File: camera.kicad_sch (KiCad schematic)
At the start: 23 parts, among them J3 WE_68715014522, U10 PI4MSD5V9540BUEX, U11 AP7340-18FS4-7

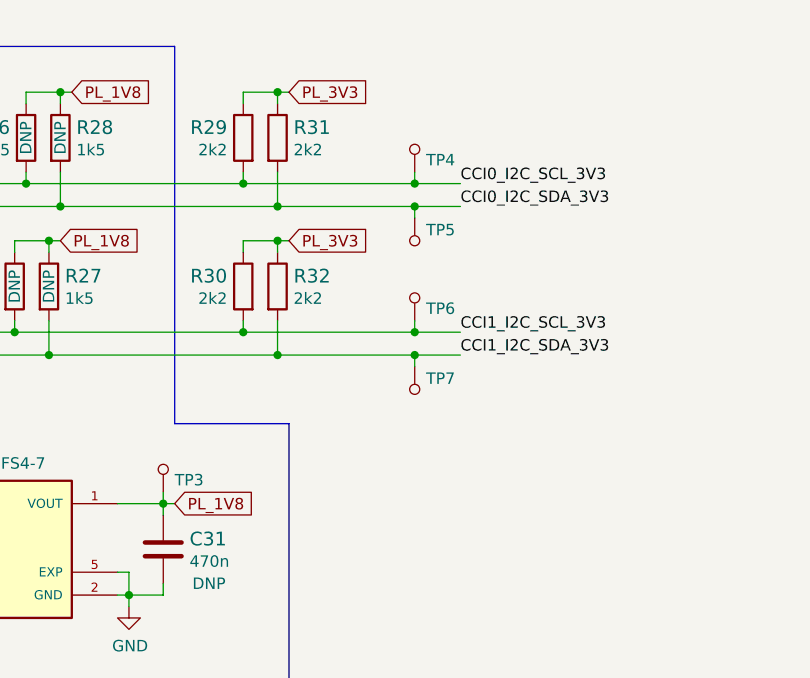
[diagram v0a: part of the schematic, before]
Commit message: Added cosmetic changes to schematics (e.g. position of labels, designators)
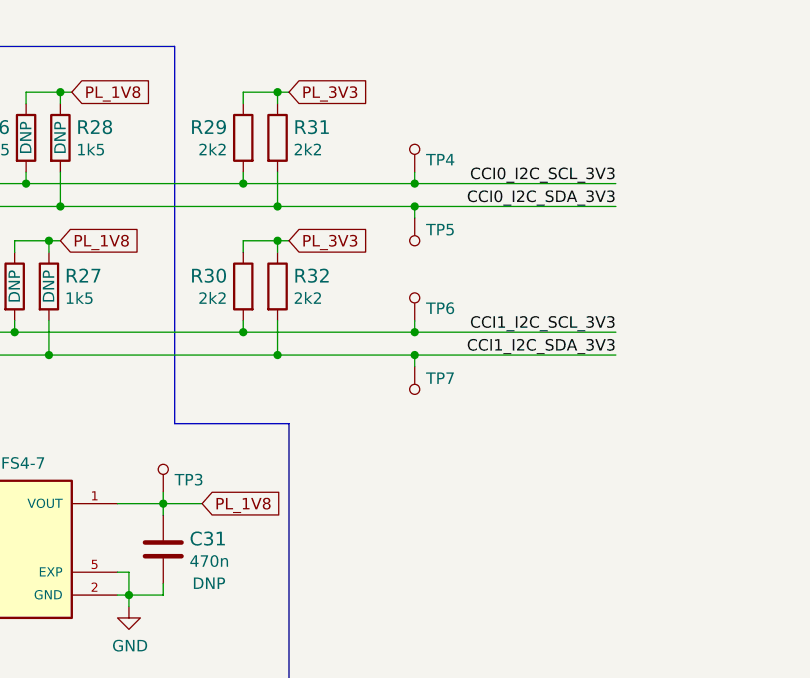
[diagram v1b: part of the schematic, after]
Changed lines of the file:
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@@
     (stroke (width 0) (type default) (color 0 0 0 0))
   )
-  (wire (pts (xy 111.76 149.86) (xy 113.03 149.86))
+  (wire (pts (xy 111.76 149.86) (xy 116.078 149.86))
     (stroke (width 0) (type default) (color 0 0 0 0))
   )
@@
     (stroke (width 0) (type default) (color 0 0 0 0))
   )
-  (wire (pts (xy 139.7 133.35) (xy 144.78 133.35))
+  (wire (pts (xy 139.7 133.35) (xy 162.052 133.35))
     (stroke (width 0) (type default) (color 0 0 0 0))
   )
@@
     (stroke (width 0) (type default) (color 0 0 0 0))
   )
-  (wire (pts (xy 139.7 116.84) (xy 144.78 116.84))
+  (wire (pts (xy 139.7 116.84) (xy 162.052 116.84))
     (stroke (width 0) (type default) (color 0 0 0 0))
   )
@@
     (stroke (width 0) (type default) (color 0 0 0 0))
   )
-  (wire (pts (xy 139.7 114.3) (xy 144.78 114.3))
-    (stroke (width 0) (type default) (color 0 0 0 0))
-  )
-  (wire (pts (xy 139.7 130.81) (xy 144.78 130.81))
+  (wire (pts (xy 139.7 114.3) (xy 162.052 114.3))
+    (stroke (width 0) (type default) (color 0 0 0 0))
+  )
+  (wire (pts (xy 139.7 130.81) (xy 162.052 130.81))
     (stroke (width 0) (type default) (color 0 0 0 0))
   )
@@
     (effects (font (size 1.27 1.27)) (justify left bottom))
   )
-  (label "CCI0_I2C_SCL_3V3" (at 144.78 114.3 0)
-    (effects (font (size 1.27 1.27)) (justify left bottom))
-  )
-  (label "CCI1_I2C_SDA_3V3" (at 144.78 133.35 0)
-    (effects (font (size 1.27 1.27)) (justify left bottom))
+  (label "CCI0_I2C_SCL_3V3" (at 162.052 114.3 180)
+    (effects (font (size 1.27 1.27)) (justify right bottom))
+  )
+  (label "CCI1_I2C_SDA_3V3" (at 162.052 133.35 180)
+    (effects (font (size 1.27 1.27)) (justify right bottom))
   )
   (label "CCI1_I2C_SDA_3V3" (at 190.5 124.46 0)
     (effects (font (size 1.27 1.27)) (justify left bottom))
   )
-  (label "CCI1_I2C_SCL_3V3" (at 144.78 130.81 0)
-    (effects (font (size 1.27 1.27)) (justify left bottom))
-  )
-  (label "CCI0_I2C_SDA_3V3" (at 144.78 116.84 0)
-    (effects (font (size 1.27 1.27)) (justify left bottom))
+  (label "CCI1_I2C_SCL_3V3" (at 162.052 130.81 180)
+    (effects (font (size 1.27 1.27)) (justify right bottom))
+  )
+  (label "CCI0_I2C_SDA_3V3" (at 162.052 116.84 180)
+    (effects (font (size 1.27 1.27)) (justify right bottom))
   )
   (label "CCI0_I2C_SDA_3V3" (at 190.5 119.38 0)
@@
     (effects (font (size 1.27 1.27)) (justify left bottom))
   )
-  (global_label "PL_1V8" (shape input) (at 113.03 149.86 0) (fields_autoplaced)
+  (global_label "PL_1V8" (shape input) (at 116.078 149.86 0) (fields_autoplaced)
     (effects (font (size 1.27 1.27)) (justify left))
-    (property "Intersheet References" "${INTERSHEET_REFS}" (id 0) (at 0 0 0)
+    (property "Intersheet References" "${INTERSHEET_REFS}" (id 0) (at 3.048 0 0)
       (effects (font (size 1.27 1.27)) hide)
     )

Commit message: Bump date and revision
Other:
- title: Camera interface -> Kria K26 Devboard
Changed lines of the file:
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@@
   (paper "A4")
   (title_block
-    (title "Camera interface")
-    (date "2022-07-25")
-    (rev "1.1.0")
+    (title "Kria K26 Devboard")
+    (date "2023-02-15")
+    (rev "1.1.1")
     (comment 1 "www.antmicro.com")
     (comment 2 "Antmicro Ltd.")

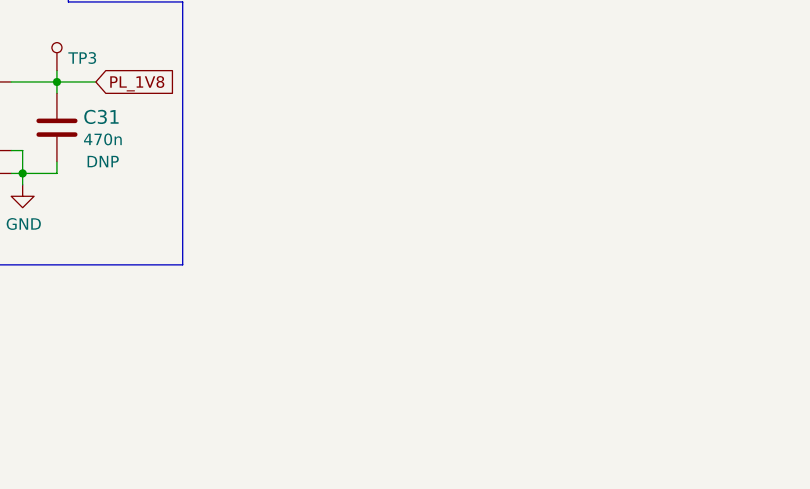
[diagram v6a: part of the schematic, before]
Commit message: Add decoupling to cammera and DP connector, schematic cleanup
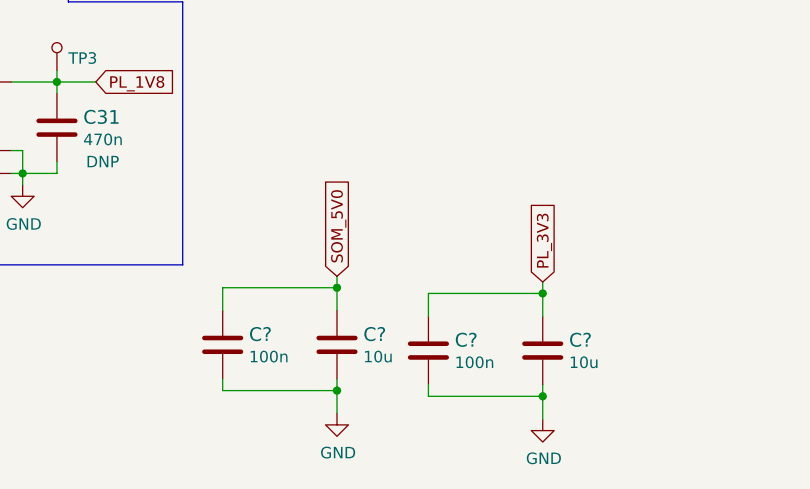
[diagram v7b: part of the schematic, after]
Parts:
- added C? (x2): C_10u_0603, kria-k26-devboard-footprints:0603-cap, symbol kria-k26-devboard:C_10u_0603
- added C? (x2): C_100n_0402, kria-k26-devboard-footprints:0402-cap, symbol kria-k26-devboard:C_100n_0402
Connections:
- net GND: now also C?.2, C?.2, C?.2, C?.2
- net PL_3V3: now also C?.1, C?.1
- net SOM_5V0: now also C?.1, C?.1
